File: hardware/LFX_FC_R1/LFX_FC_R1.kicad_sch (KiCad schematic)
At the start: 0 parts

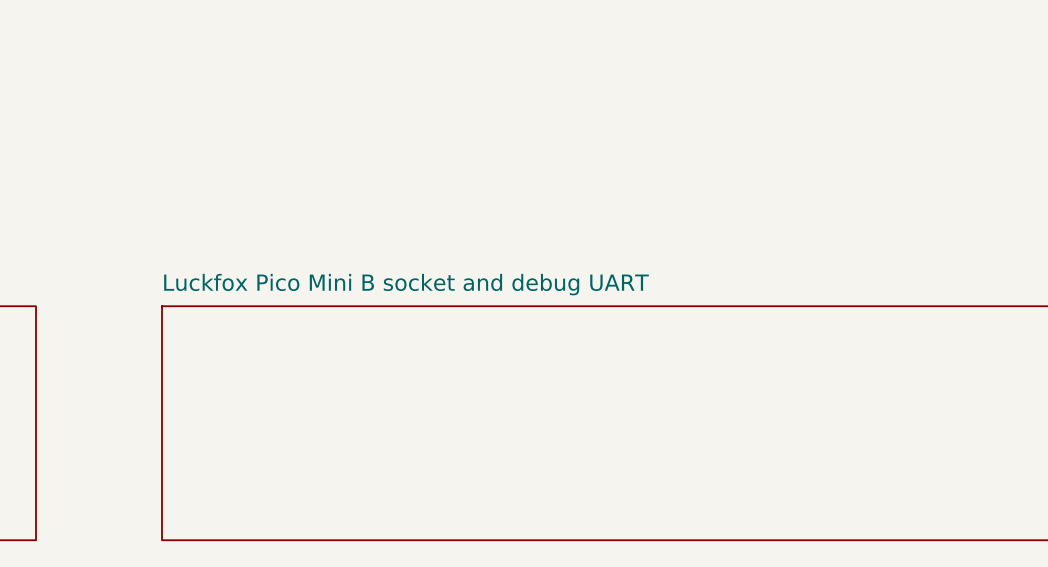
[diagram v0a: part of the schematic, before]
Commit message: hardware: RC receiver port (ELRS/CRSF) on UART2 instead of debug console
- J4 becomes a 4-pin JST-SH RC port: 1 5V, 2 GND, 3 TX (to receiver RX),
  4 RX (from receiver TX, CRSF 420000 baud), same order as the GPS port
- R24 1k pull-up on RC_RX to the module's 3V3 (pin 3): ESP-based ELRS
  receivers stall in the bootloader if that line is low at power-up
  (expresslrs.org receiver wiring guide)
- TP5/TP6 on RC_TX/RC_RX: console tap with the receiver unplugged
- UART2 has its own fractional divider (clk-rv1106.c:441), 420000 x 16 =
  24 MHz x 7/25; not yet measured
- docs: RC path goes through Linux, MCU failsafe on heartbeat loss; the
  console has to leave UART2 in software (fiq-debugger, earlycon)
- ERC 0, DRC 0 / 0 unconnected / 0 parity errors

Co-Authored-By: Claude Opus 5.5 <noreply@anthropic.com>
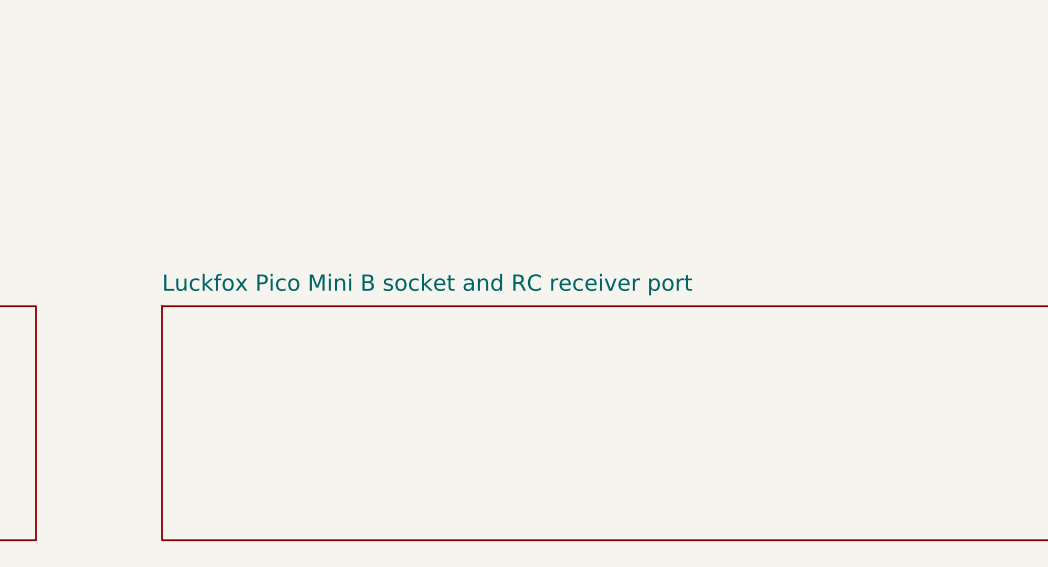
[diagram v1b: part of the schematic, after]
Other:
- sheet Luckfox Pico Mini B socket and debug UART renamed Luckfox Pico Mini B socket and RC receiver port
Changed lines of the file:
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@@
 		(stroke (width 0.2) (type solid))
 		(fill (color 0 0 0 0.0))
-		(property "Sheetname" "Luckfox Pico Mini B socket and debug UART"
+		(property "Sheetname" "Luckfox Pico Mini B socket and RC receiver port"
 			(at 199 68.5 0)
 			(effects (font (size 1.8 1.8)) (justify left bottom))

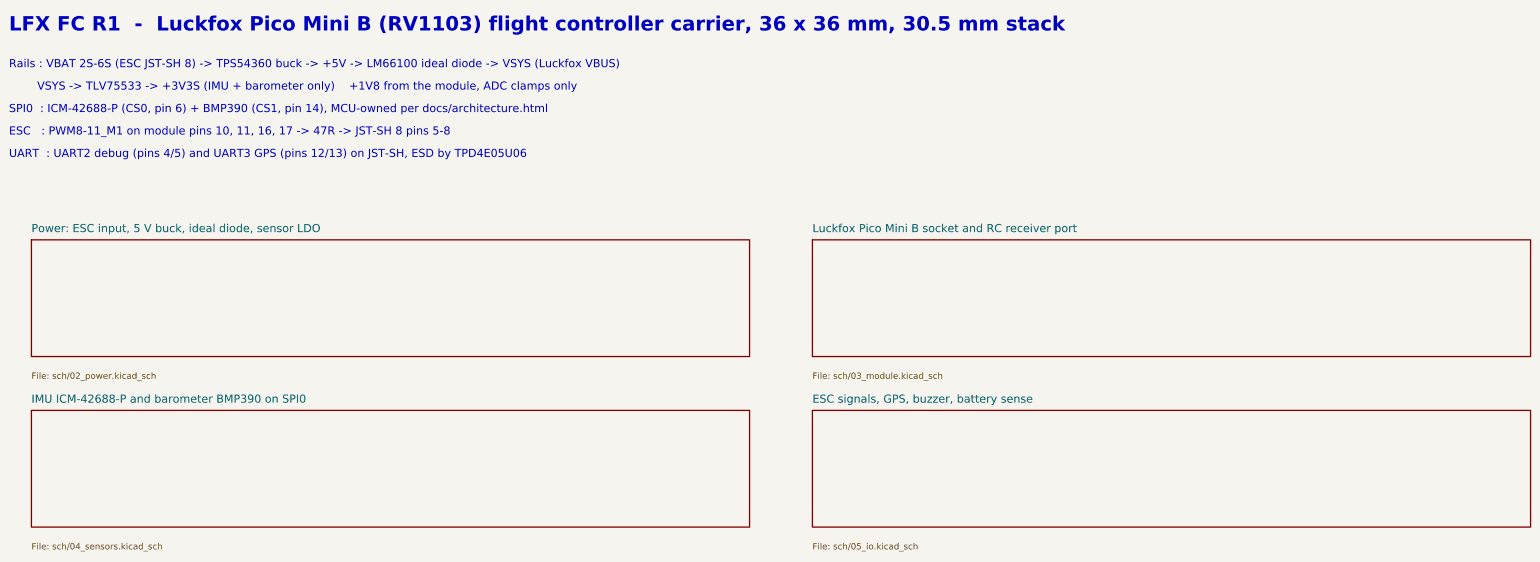
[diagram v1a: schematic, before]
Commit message: hardware: LFX_LTE_R1 stacked LTE + GNSS board, FC link on J5
New 46 x 46 mm board hardware/LFX_LTE_R1 (same 39 mm M3 pattern, stacks on
the flight controller, all parts on the top side):
- Lierda NT26-KCN E LTE Cat.1 bis + GNSS (order the GPS + BDS variant);
  symbol and LCC/LGA-109 land pattern drawn from the Lierda hardware design
  manual Rev1.0 (table 2-5, fig. 2-2, fig. 8-3)
- TLV62569 buck +5V -> 3.8 V (modem VBAT 3.3-4.5 V), In2 +3V8 plane,
  2 x 47 uF + 100n / 33p / 8p2 at VBAT; TLV75533 3.3 V for the translators
- UART 3.3 <-> 1.8 V by 2 x SN74LVC1T45 (Hi-Z while the modem is off)
- Luckfox reflashes the modem: RESET_N via AO3400A, USB_BOOT via 1k from the
  1.8 V BOOT pin; USB / debug test pads for a PC rescue
- hinged nano-SIM with 22R / 33p / TPD4E05U06, LTE and GNSS U.FL with pi
  match, 50 ohm 0.35 mm feeds, active GNSS antenna bias
- ERC 0, DRC 0 violations / 0 unconnected / 0 parity

LFX_FC_R1 stays 46 x 46 mm:
- J5 GPS (JST-SH 4) -> LTE board link (JST-SH 10): 5V x2, GND x2, UART3,
  RESET (pin 18), BOOT (pin 20), buzzer gate, ESC current
- buzzer gate and ESC current now come from the modem's GPIO1 / ADC0
- ERC 0, DRC 0 violations / 0 unconnected / 0 parity

Shared: NT26-KCN and SIM_Card_Shield in the LFX library, stacked symbol
pins in gen_sch, route_pcb creates pcb/.  README and architecture docs
updated.

Co-Authored-By: Claude Opus 5.5 <noreply@anthropic.com>
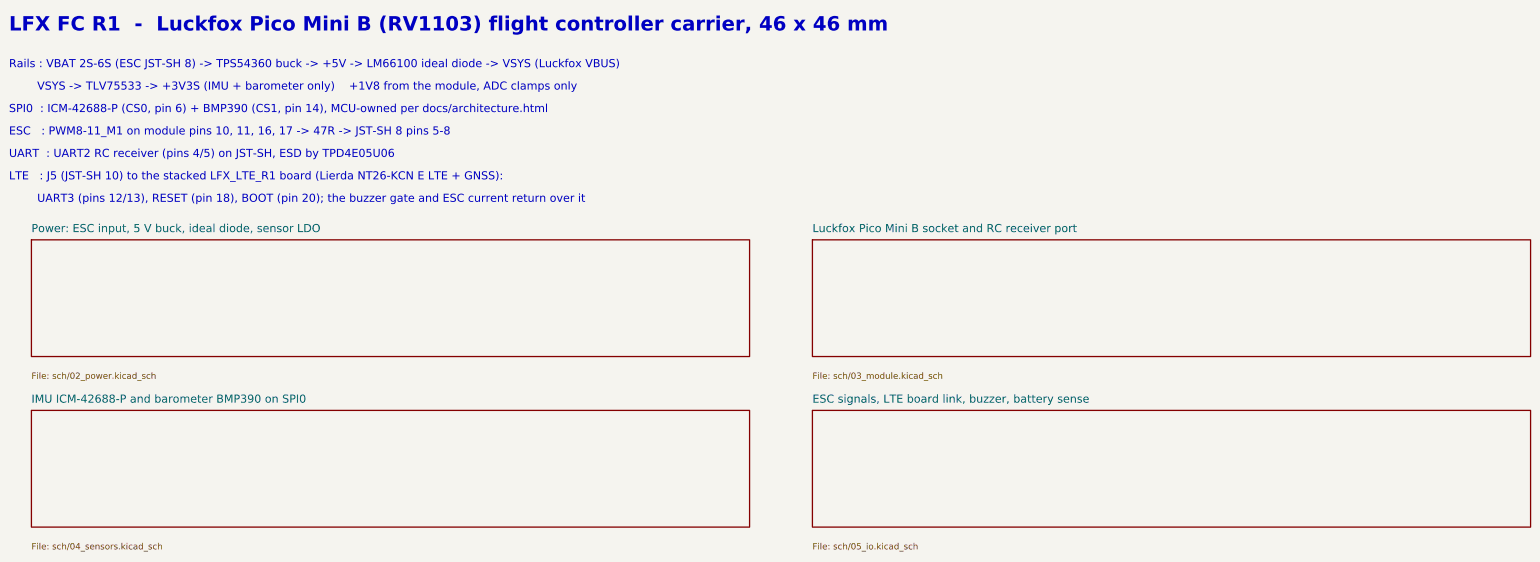
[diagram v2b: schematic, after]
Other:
- sheet ESC signals, GPS, buzzer, battery sense renamed ESC signals, LTE board link, buzzer, battery sense
- note added: "LFX FC R1 - Luckfox Pico Mini B (RV1103) flight controller carrier, 46 x 46 mm"
- note added: "LTE : J5 (JST-SH 10) to the stacked LFX_LTE_R1 board (Lierda NT26-KCN E LTE + GNSS):"
- note added: "UART : UART2 RC receiver (pins 4/5) on JST-SH, ESD by TPD4E05U06"
- note added: "UART3 (pins 12/13), RESET (pin 18), BOOT (pin 20); the buzzer gate and ESC current return over it"
- note removed: "LFX FC R1 - Luckfox Pico Mini B (RV1103) flight controller carrier, 36 x 36 mm, 30.5 mm stack"
- note removed: "UART : UART2 debug (pins 4/5) and UART3 GPS (pins 12/13) on JST-SH, ESD by TPD4E05U06"
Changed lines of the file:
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@@
 		(comment 2 "Generated from scripts/design.py")
 	)
-	(text "LFX FC R1  -  Luckfox Pico Mini B (RV1103) flight controller carrier, 36 x 36 mm, 30.5 mm stack"
+	(text "LFX FC R1  -  Luckfox Pico Mini B (RV1103) flight controller carrier, 46 x 46 mm"
 		(at 20 24 0)
 		(effects (font (size 3.2 3.2) (bold yes)) (justify left bottom))
@@
 		(effects (font (size 1.8 1.8)) (justify left bottom))
 	)
-	(text "UART  : UART2 debug (pins 4/5) and UART3 GPS (pins 12/13) on JST-SH, ESD by TPD4E05U06"
+	(text "UART  : UART2 RC receiver (pins 4/5) on JST-SH, ESD by TPD4E05U06"
 		(at 20 52 0)
+		(effects (font (size 1.8 1.8)) (justify left bottom))
+	)
+	(text "LTE   : J5 (JST-SH 10) to the stacked LFX_LTE_R1 board (Lierda NT26-KCN E LTE + GNSS):"
+		(at 20 57 0)
+		(effects (font (size 1.8 1.8)) (justify left bottom))
+	)
+	(text "        UART3 (pins 12/13), RESET (pin 18), BOOT (pin 20); the buzzer gate and ESC current return over it"
+		(at 20 62 0)
 		(effects (font (size 1.8 1.8)) (justify left bottom))
 	)
@@
 		(stroke (width 0.2) (type solid))
 		(fill (color 0 0 0 0.0))
-		(property "Sheetname" "ESC signals, GPS, buzzer, battery sense"
+		(property "Sheetname" "ESC signals, LTE board link, buzzer, battery sense"
 			(at 199 106.5 0)
 			(effects (font (size 1.8 1.8)) (justify left bottom))
